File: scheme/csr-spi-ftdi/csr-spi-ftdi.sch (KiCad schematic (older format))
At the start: 23 parts, among them P1 CONN_5X2, U1 LM1117-3.3, U2 LM1117-1.8, U3 FT232RL

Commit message: a
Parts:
- removed C4, C6: 10uF, symbol CP1
- removed JP1: VIO SELECT JUMPER, symbol JUMPER3
- removed P1: CONN_5X2, symbol CONN_5X2
- removed U1: LM1117-3.3, SOT223, symbol LM1117
- removed U2: LM1117-1.8, SOT223, symbol LM1117
- removed USB1: USB_B_5S, ~, symbol USB_B_5S
- added C?: 4u7, symbol C
- added P?: USB_B, symbol USB_B
- added P?: CONN_02X05, symbol CONN_02X05
- added U?: MCP1703T-3302E/CB, symbol MCP1703T-3302E/CB
- C?: value 0.1uF -> 4u7
- R2, R3: value 470 -> 1k
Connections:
- wire segments 77 -> 69

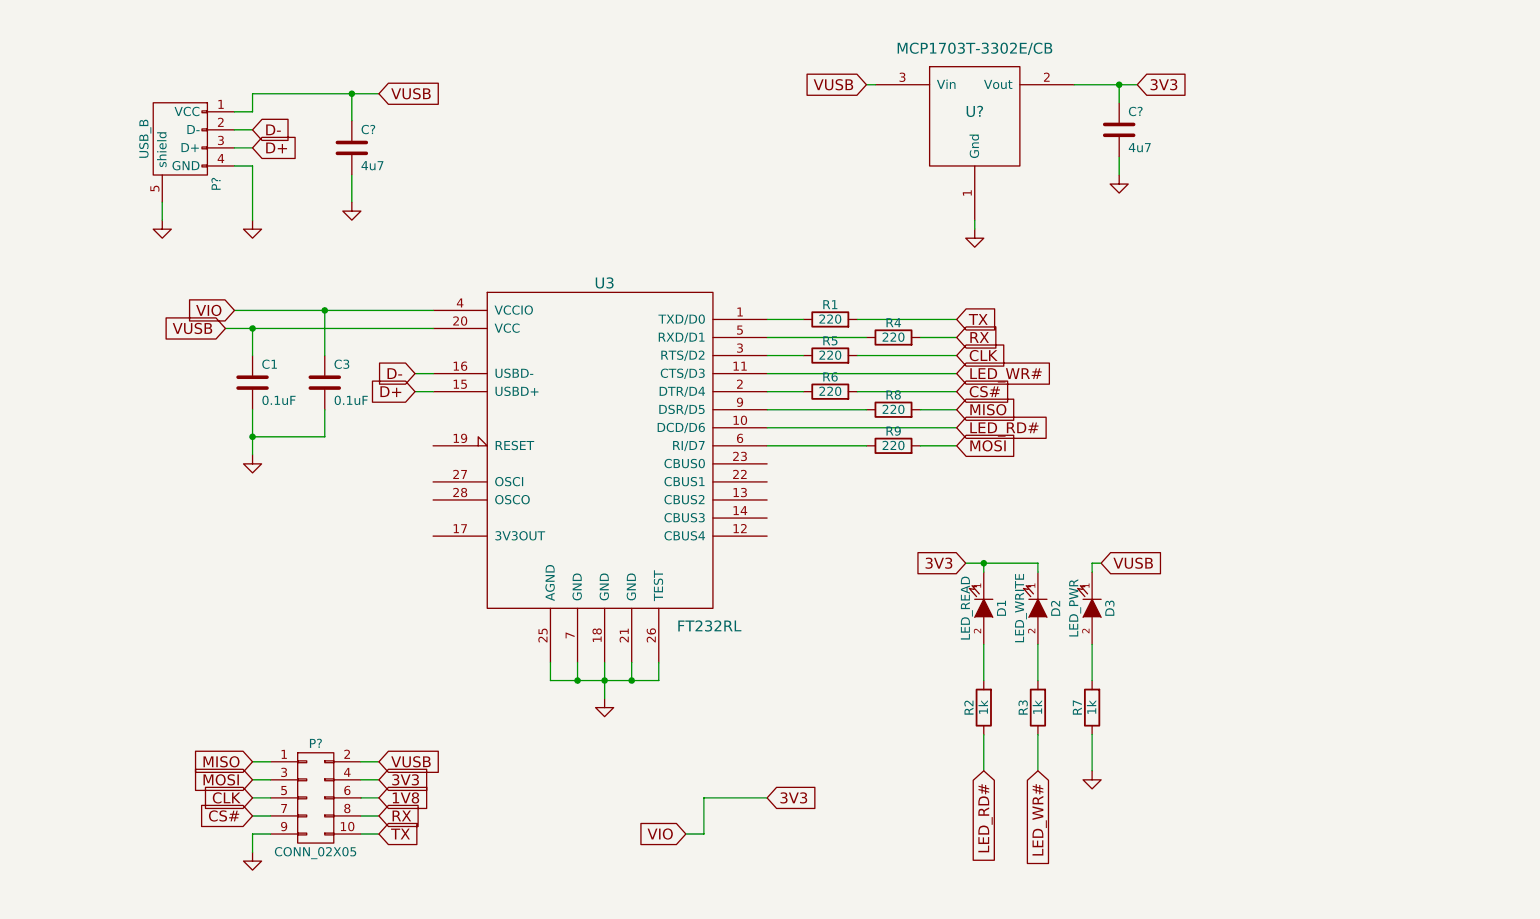
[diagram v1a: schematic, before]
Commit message: Assigned footprints to components.
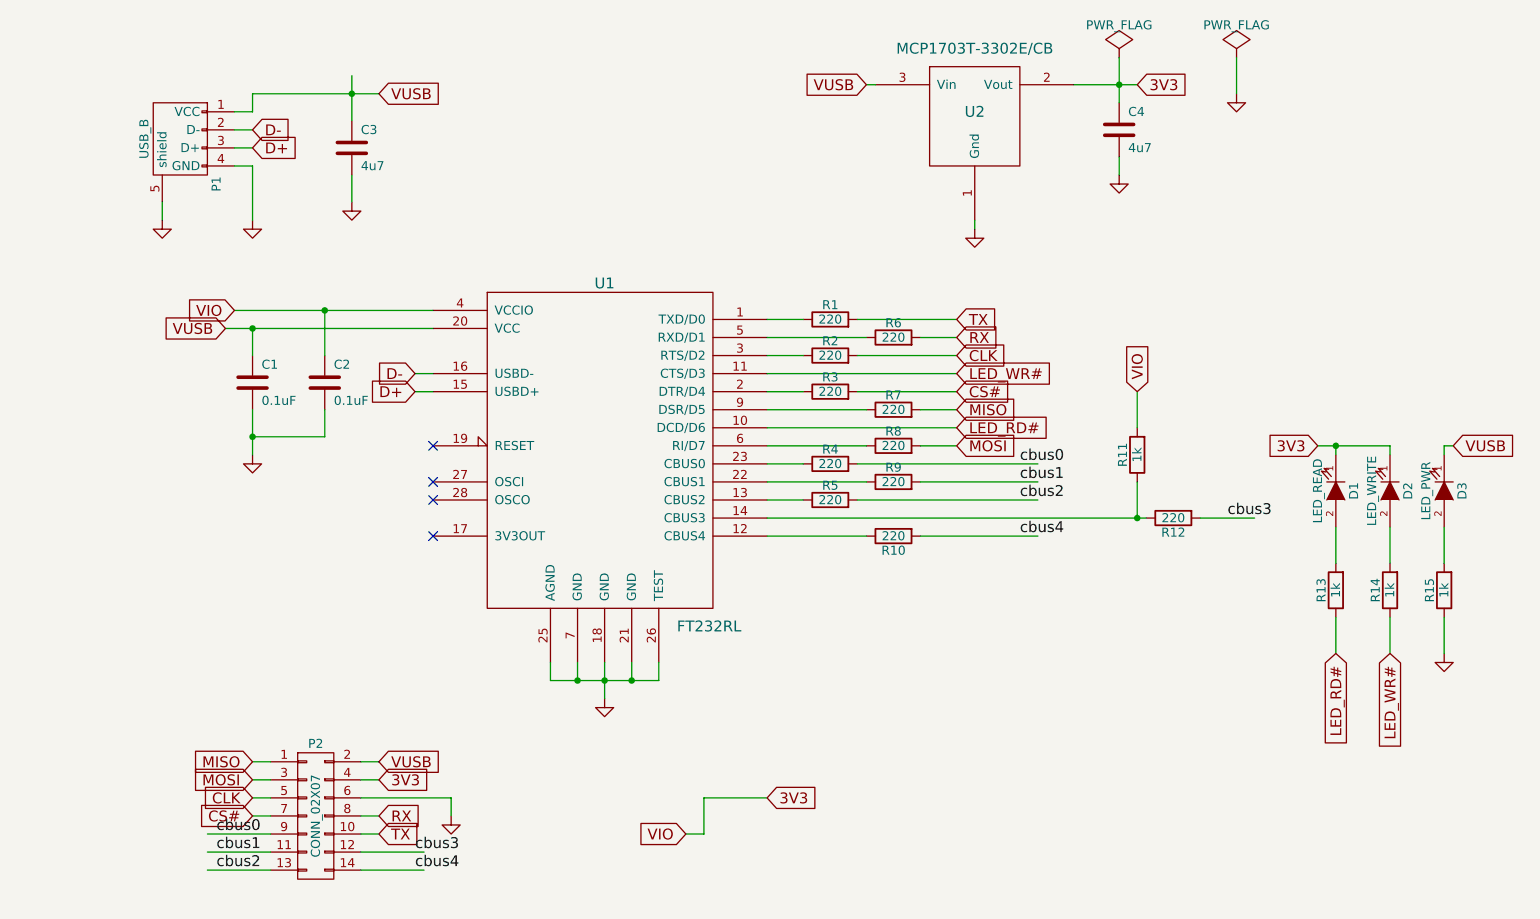
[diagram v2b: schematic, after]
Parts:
- removed P?: CONN_02X05, symbol CONN_02X05
- added P2: CONN_02X07, Pin_Headers:Pin_Header_Angled_2x07, symbol CONN_02X07
- added R10, R12, R4, R5, R9: 220, Resistors_SMD:R_0805, symbol R
- added R11: 1k, Resistors_SMD:R_0805, symbol R
- C1: footprint (none) -> Capacitors_SMD:C_0805
- C2: renamed from C3; footprint (none) -> Capacitors_SMD:C_0805
- C3, C4: renamed from C?; footprint (none) -> Capacitors_SMD:C_0805
- D1, D2, D3: footprint (none) -> LEDs:LED-5MM
- P1: renamed from P?; footprint (none) -> Connect:USB_B
- R1: footprint (none) -> Resistors_SMD:R_0805
- R13: renamed from R2; footprint (none) -> Resistors_SMD:R_0805
- R14: renamed from R3; footprint (none) -> Resistors_SMD:R_0805
- R15: renamed from R7; footprint (none) -> Resistors_SMD:R_0805
- R2: renamed from R5; footprint (none) -> Resistors_SMD:R_0805
- R3: renamed from R6; footprint (none) -> Resistors_SMD:R_0805
- R6: renamed from R4; footprint (none) -> Resistors_SMD:R_0805
- R7: renamed from R8; footprint (none) -> Resistors_SMD:R_0805
- R8: renamed from R9; footprint (none) -> Resistors_SMD:R_0805
- U1: renamed from U3; footprint (none) -> Housings_SSOP:SSOP-28_5.3x10.2mm_Pitch0.65mm
- U2: renamed from U?; footprint (none) -> TO_SOT_Packages_SMD:SOT-23_Handsoldering
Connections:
- net labels added: cbus0, cbus1, cbus2, cbus3, cbus4
- net labels removed: 1V8
- wire segments 69 -> 86
- no-connect marks 0 -> 4
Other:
- moved on the sheet: D1, D2, D3, R13, R14, R15

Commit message: a
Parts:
- removed P2: CONN_02X07, Pin_Headers:Pin_Header_Angled_2x07, symbol CONN_02X07
- removed R1, R10, R12, R2, R3, R4, R5, R6, R7, R8, R9: 220, Resistors_SMD:R_0805, symbol R
- removed R11: 1k, Resistors_SMD:R_0805, symbol R
- added P?: CONN_02X05, symbol CONN_02X05
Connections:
- net labels removed: cbus0, cbus1, cbus2, cbus3, cbus4
- wire segments 86 -> 65
- no-connect marks 4 -> 9

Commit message: Finished debug PCB.
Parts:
- removed P?: CONN_02X05, symbol CONN_02X05
- added P10, P11, P2, P3, P4, P5, P6, P7, P8, P9: TST, Measurement_Points:Measurement_Point_Round-SMD-Pad_Small, symbol TST
- added R1, R2, R3, R5, R7, R8: 220, Resistors_SMD:R_0805, symbol R
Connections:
- net 3V3: now also P8.1
- net CLK: now also P4.1, R2.2; no longer U1.3 (RTS/D2)
- net CS#: now also P5.1, R3.2; no longer U1.2 (DTR/D4)
- net GND: now also P6.1, P9.1
- net MISO: now also P2.1, R7.2; no longer U1.9 (DSR/D5)
- net MOSI: now also P3.1, R8.2; no longer U1.6 (RI/D7)
- net RX: now also P10.1, R5.2; no longer U1.5 (RXD/D1)
- net TX: now also P11.1, R1.2; no longer U1.1 (TXD/D0)
- net VUSB: now also P7.1
- new net: R1.1, U1.1 (TXD/D0)
- new net: R3.1, U1.2 (DTR/D4)
- new net: R2.1, U1.3 (RTS/D2)
- new net: R5.1, U1.5 (RXD/D1)
- new net: R8.1, U1.6 (RI/D7)
- new net: R7.1, U1.9 (DSR/D5)
- no-connect marks 9 -> 4
